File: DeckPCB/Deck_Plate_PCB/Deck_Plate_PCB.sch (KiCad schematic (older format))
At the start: 76 parts, among them J1 Raspberry_Pi_2_3, J2 NASA_Telemetry_Interface, J3 NASA PWR_Interface, J8 Board_to_Board, J9 Power, P1 Digital, P10 CONN_01X01, P11 CONN_01X01, P12 CONN_01X01, P13 CONN_01X01, P2 Power, P3 Analog, P4 Analog, P5 PWM, P6 PWM, P7 Communication, P8 CONN_01X01, P9 CONN_01X01, Q2 2N7000, Q3 2N7000, U1 LF356, U10 MAX1044, U11 LF356, U12 LF356, U2 LM2576T-5, U3 D24V25F9, U4 LF356, U5 LM2576T-5, U6 SF_Logic_Level_Conv, U7 Lidar_RangeFinder, U8 ADXL377, U9 TTL_Camera

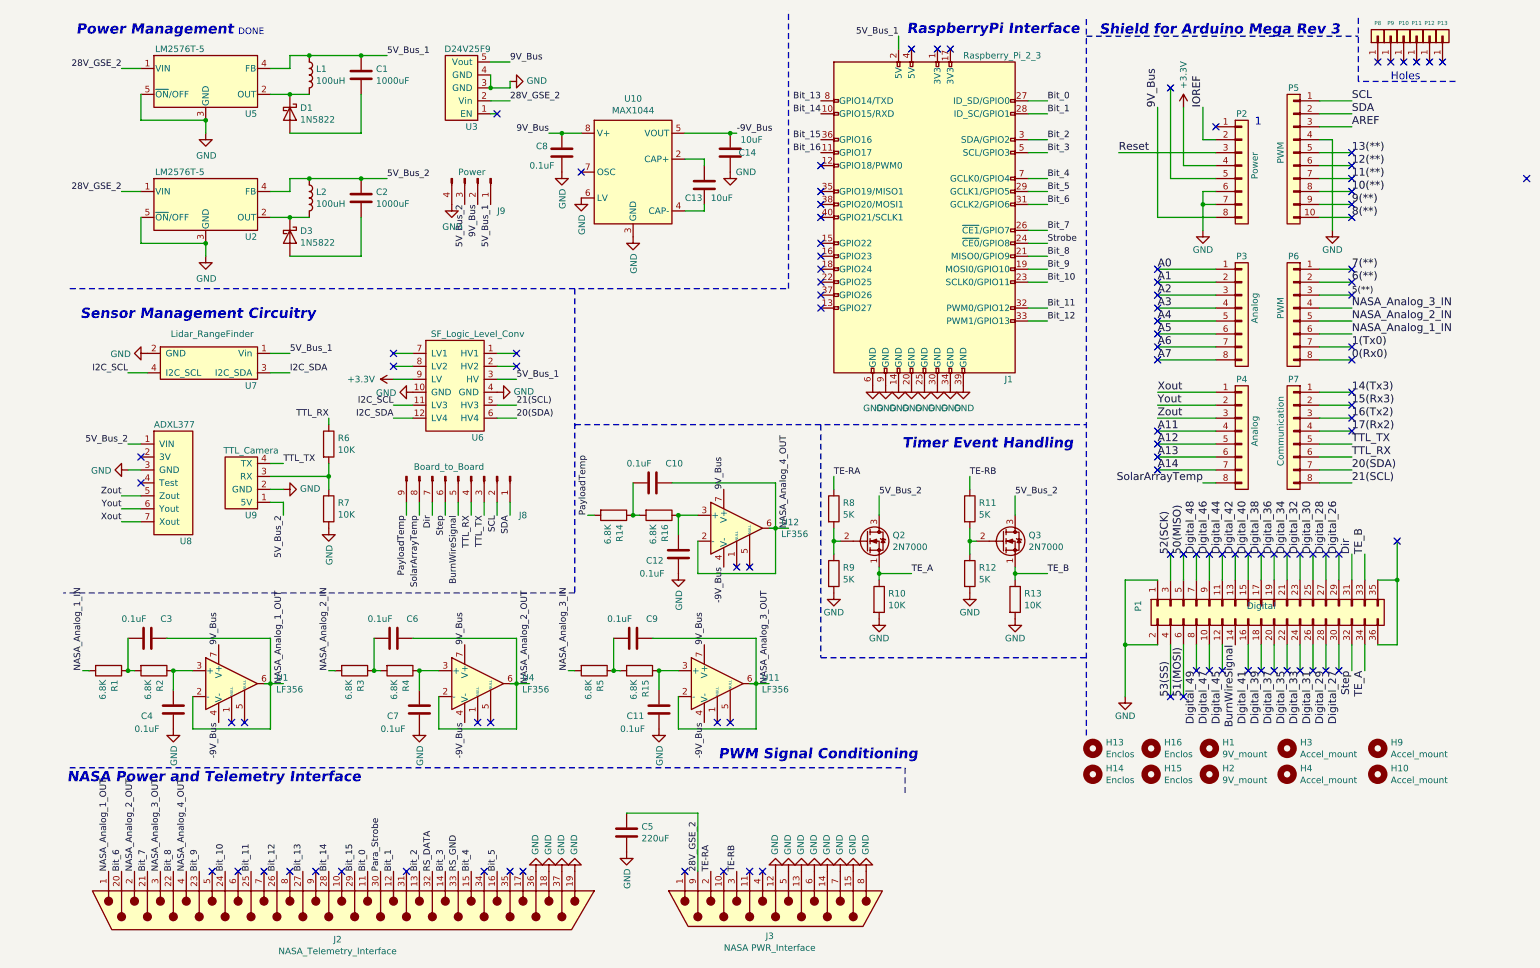
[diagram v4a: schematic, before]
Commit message: Updated PCB for NASA analog lines and signal conditioning circuitry. Added Gerber file ZIP for DECK_PLATE_MAIN
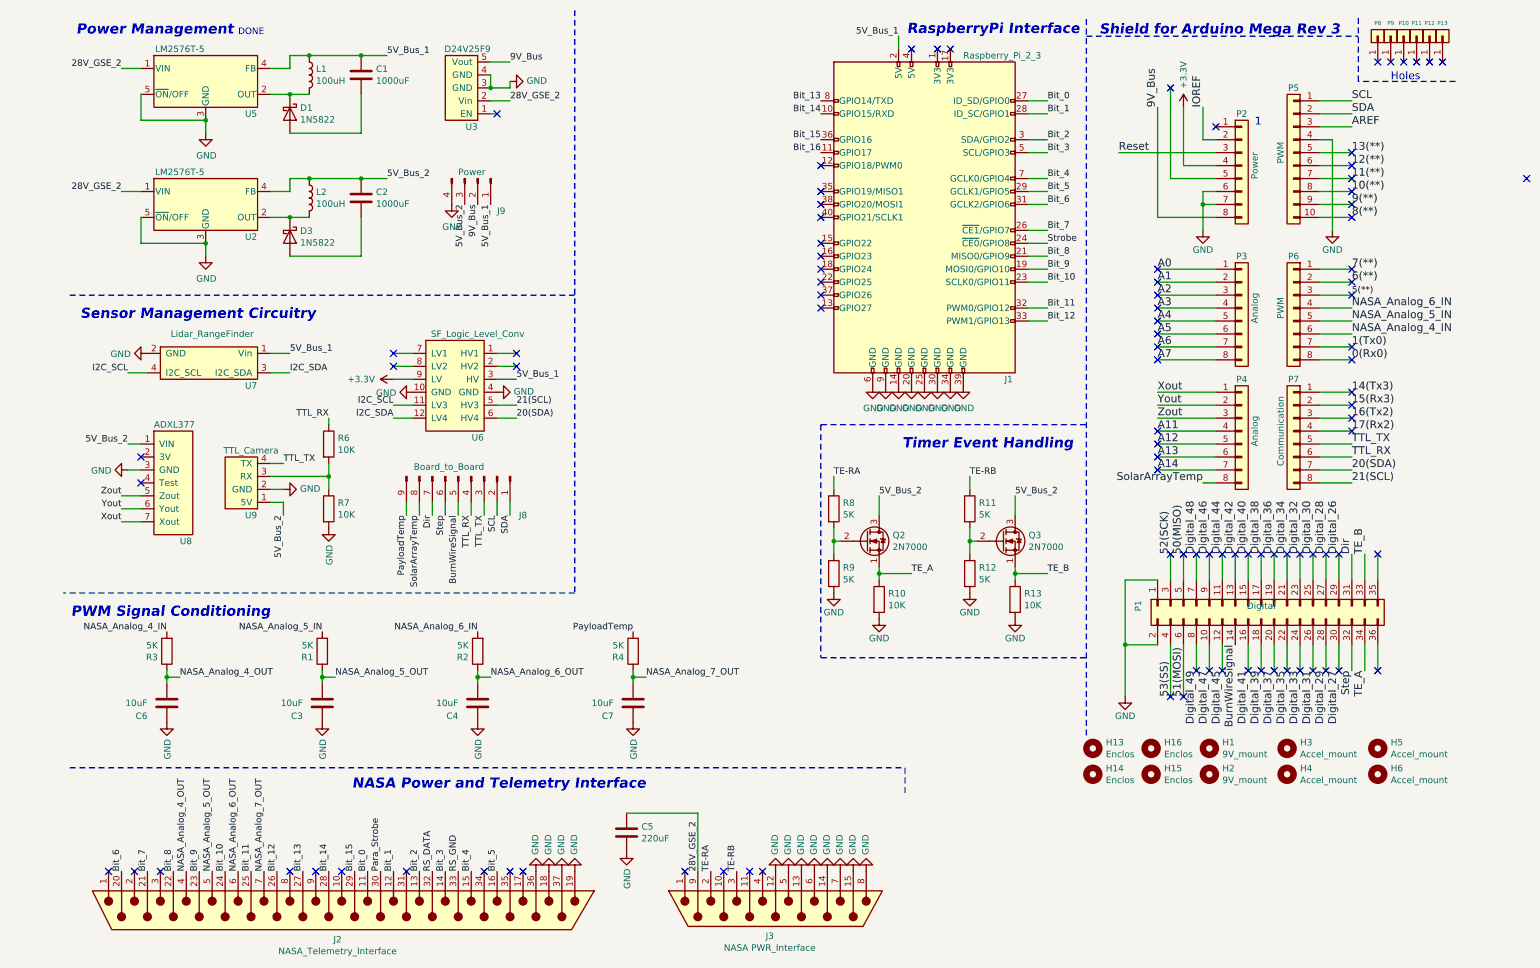
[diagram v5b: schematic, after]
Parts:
- removed C10, C11, C12, C8, C9: 0.1uF, Capacitor_THT:C_Axial_L3.8mm_D2.6mm_P7.50mm_Horizontal, symbol Device:C
- removed C13, C14: 10uF, Capacitor_THT:C_Axial_L3.8mm_D2.6mm_P7.50mm_Horizontal, symbol Device:C
- removed H10, H9: Accel_mount, MountingHole:MountingHole_2.5mm, symbol Mechanical:MountingHole
- removed R14, R15, R16, R5: 6.8K, Resistor_THT:R_Axial_DIN0207_L6.3mm_D2.5mm_P10.16mm_Horizontal, symbol Device:R
- removed U1, U11, U12, U4: LF356, Package_DIP:DIP-8_W7.62mm, symbol Amplifier_Operational:LF356
- removed U10: MAX1044, Package_DIP:DIP-8_W7.62mm, symbol Regulator_SwitchedCapacitor:MAX1044
- added H5, H6: Accel_mount, Deck_Plate_PCB:Accel_MountingHole_2.5mm, symbol Mechanical:MountingHole
- C3, C4, C6, C7: value 0.1uF -> 10uF
- H1, H2: footprint MountingHole:MountingHole_2.2mm_M2 -> Deck_Plate_PCB:9V_MountingHole_2.2mm
- H3, H4: footprint MountingHole:MountingHole_2.5mm -> Deck_Plate_PCB:Accel_MountingHole_2.5mm
- R1, R2, R3, R4: value 6.8K -> 5K
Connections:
- net GND: now also C3.1, C4.1, C6.1, C7.1; no longer C4.2, C7.2
- net NASA_Analog_4_OUT: now also C6.2, R3.1
- net PayloadTemp: now also R4.2
- net at P1.35 (Pin_35): no longer P1.36 (Pin_36)
- net NASA_Analog_5_OUT: now reaches J2.5
- net NASA_Analog_5_OUT: now also C3.2, R1.1
- net NASA_Analog_6_OUT: now reaches J2.6
- net NASA_Analog_6_OUT: now also C4.2, R2.1
- net NASA_Analog_7_OUT: now reaches J2.7
- net NASA_Analog_7_OUT: now also C7.2, R4.1
- net NASA_Analog_1_IN renamed NASA_Analog_4_IN
- net NASA_Analog_4_IN: now also R3.2; no longer R1.2
- net NASA_Analog_1_OUT: no longer names the net of J2.1
- net NASA_Analog_1_OUT: no longer C3.1
- net NASA_Analog_2_IN renamed NASA_Analog_5_IN
- net NASA_Analog_5_IN: now also R1.2; no longer R3.2
- net NASA_Analog_2_OUT: no longer names the net of J2.2
- net NASA_Analog_2_OUT: no longer C6.1
- net NASA_Analog_3_IN renamed NASA_Analog_6_IN
- net NASA_Analog_6_IN: now also R2.2
- net NASA_Analog_3_OUT: no longer names the net of J2.3
- no-connect marks 107 -> 99
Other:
- moved on the sheet: C6, R3

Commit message: Updated Main_Deck_Plate and Daughter_Board to fit Electronics Enclosure internal dimensions. Created all PCB Gerber files. Created all PCB PNG images. Created all PCB STEP files for mechanical integration. Implemented all design review comments and corrections.
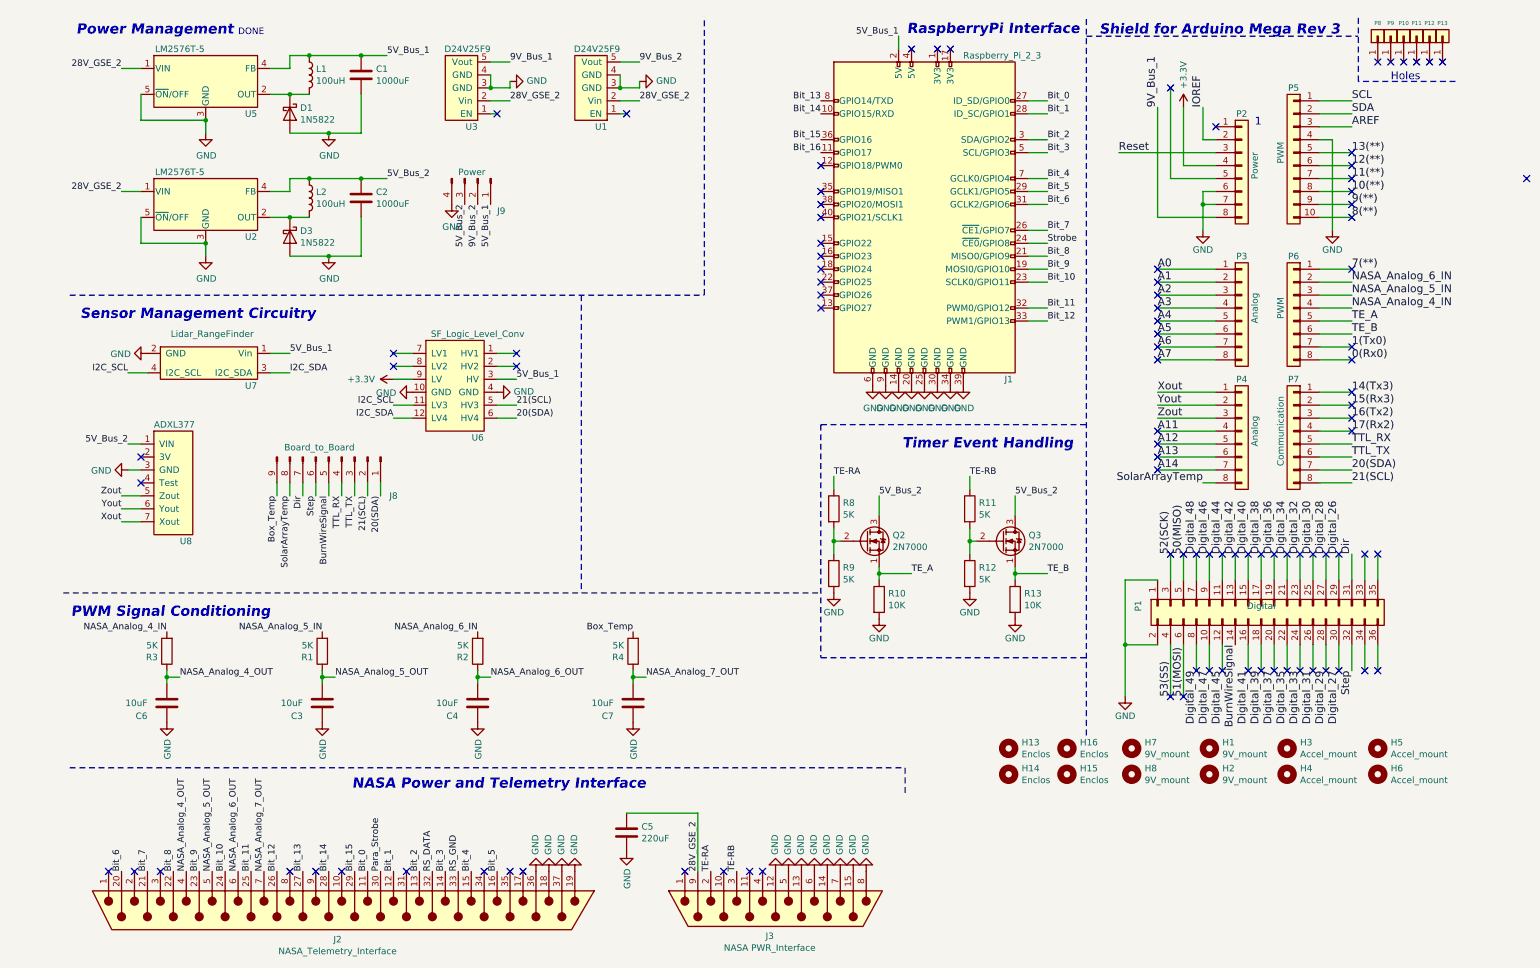
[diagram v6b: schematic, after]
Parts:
- removed R6, R7: 10K, Resistor_THT:R_Axial_DIN0207_L6.3mm_D2.5mm_P10.16mm_Horizontal, symbol Device:R
- removed U9: TTL_Camera, Connector_PinHeader_2.54mm:PinHeader_1x04_P2.54mm_Vertical, symbol Deck_Plate_PCB:TTL_Camera
- added H7, H8: 9V_mount, Deck_Plate_PCB:9V_MountingHole_2.2mm, symbol Mechanical:MountingHole
- added U1: D24V25F9, Deck_Plate_PCB:D24V25F9, symbol Deck_Plate_PCB:D24V25F9
- C3, C4, C6, C7: DigiKey P/N (none) -> 445-173370-1-ND; Manufacture P/N (none) -> FG24X7R1A106KRT06
- L1, L2: footprint Inductor_THT:L_Axial_L5.3mm_D2.2mm_P2.54mm_Vertical_Vishay_IM-1 -> Inductor_THT:L_Toroid_Vertical_L21.6mm_W9.5mm_P7.11mm_Pulse_C
- R10, R13: DigiKey P/N (none) -> RNF14FTD10K0CT-ND; Manufacture P/N (none) -> RNF14FTD10K0
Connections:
- net 5(**) is gone; now on net NASA_Analog_5_IN: P6.3 (Pin_3)
- net 6(**) is gone; now on net NASA_Analog_6_IN: P6.2 (Pin_2)
- net 20(SDA): now also J8.1 (Pin_1)
- net 21(SCL): now also J8.2 (Pin_2)
- net 28V_GSE_2: now also U1.2 (Vin)
- net GND: now also C1.2, C2.2, D1.2 (A), D3.2 (A), U1.3 (GND), U1.4 (GND)
- net NASA_Analog_4_IN: now also P6.4 (Pin_4); no longer P6.6 (Pin_6)
- net NASA_Analog_5_IN: no longer P6.5 (Pin_5)
- net NASA_Analog_6_IN: no longer P6.4 (Pin_4)
- net SCL: no longer J8.2 (Pin_2)
- net SDA: no longer J8.1 (Pin_1)
- net TE_A: now also P6.5 (Pin_5); no longer P1.34 (Pin_34)
- net TE_B: now also P6.6 (Pin_6); no longer P1.33 (Pin_33)
- net TTL_RX: now also P7.5 (Pin_5); no longer P7.6 (Pin_6)
- net TTL_TX: now also P7.6 (Pin_6); no longer P7.5 (Pin_5)
- net 9V_Bus renamed 9V_Bus_1
- net 9V_Bus_1: no longer J9.2 (Pin_2)
- net PayloadTemp renamed Box_Temp
- new net 9V_Bus_2: J9.2 (Pin_2), U1.5 (Vout)
- no-connect marks 99 -> 100
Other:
- moved on the sheet: H13, H14, H15, H16, J8
